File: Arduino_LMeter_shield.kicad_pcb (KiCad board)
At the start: 2 copper layers, 68.6 x 53.3 mm, 33 parts, among them J1 Lx, J2 Lx, J3 GPS, M1 OLED 1.3", Q1 2SC3356, SW1 Calib., U1 LTC8741, U2 74HC590

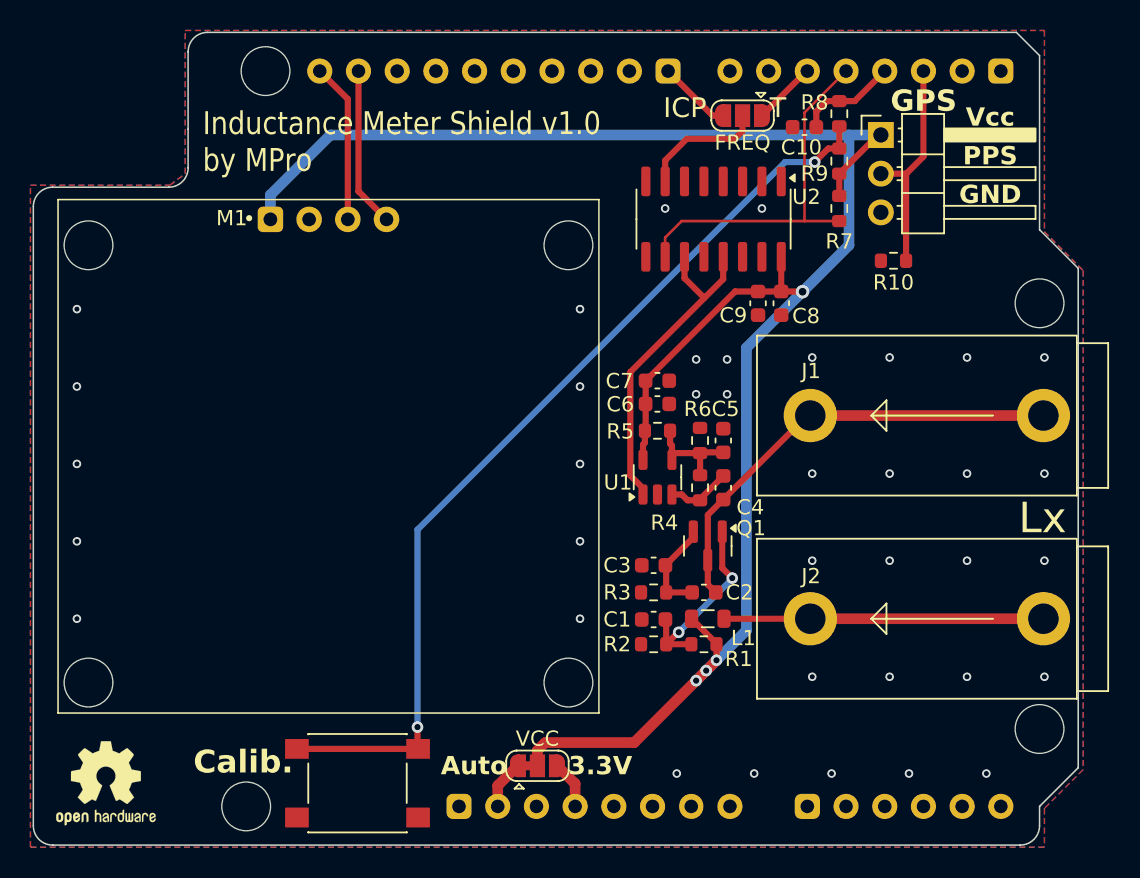
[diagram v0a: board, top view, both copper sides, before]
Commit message: OLED display footprint improved, 74HC590 chip LCSC index changed
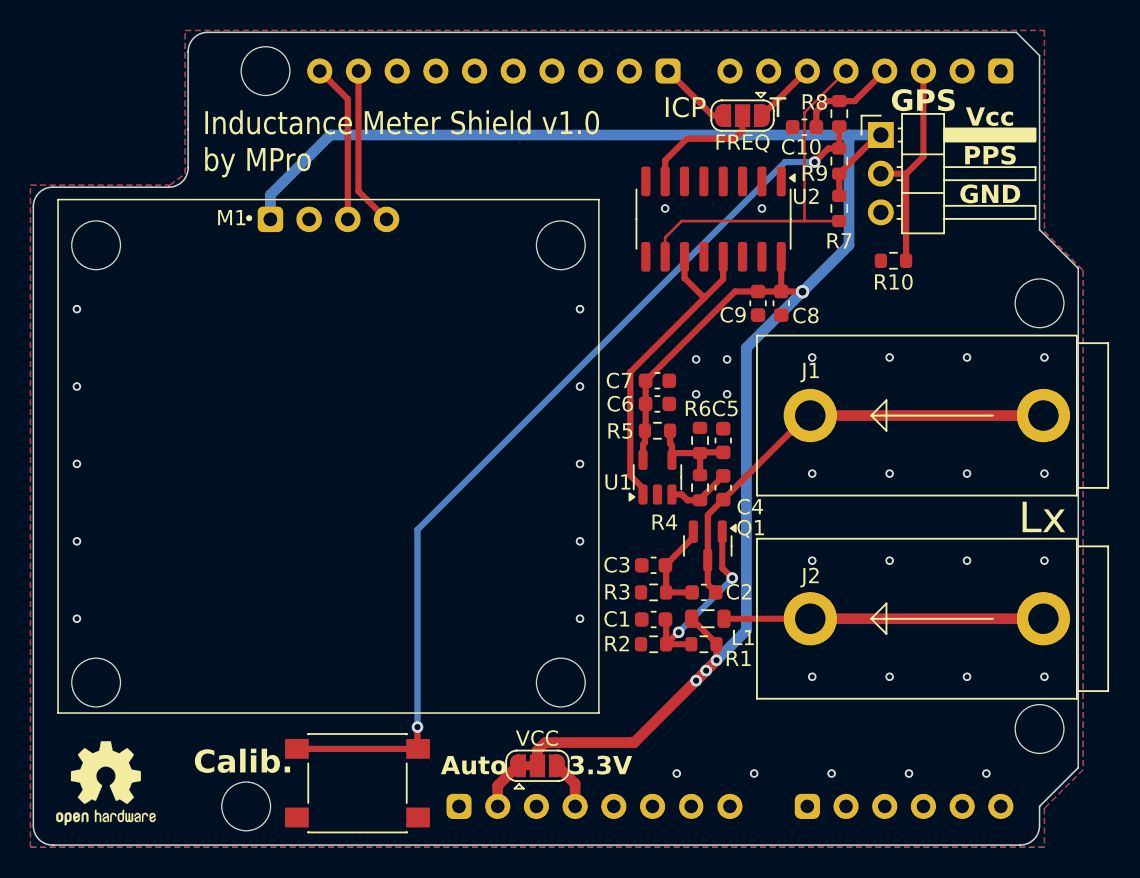
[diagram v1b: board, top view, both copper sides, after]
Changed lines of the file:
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@@
 	(title_block
 		(title "Arduino Inductance Meter shield")
-		(date "2025-04-17")
+		(date "2025-07-23")
 		(rev "1.0")
 		(company "© 2025 MPro")
@@
 		(sheetname "/")
 		(sheetfile "Arduino_LMeter_shield.kicad_sch")
-		(attr through_hole exclude_from_bom)
+		(attr through_hole exclude_from_pos_files exclude_from_bom)
 		(fp_line
 			(start 0 8.89)
@@
 			)
 		)
-		(property "Datasheet" ""
+		(property "Datasheet" "~"
 			(at 0 0 90)
 			(layer "F.Fab")
@@
 			)
 		)
-		(property "Datasheet" ""
+		(property "Datasheet" "~"
 			(at 0 0 0)
 			(layer "F.Fab")
@@
 			)
 		)
-		(property "Datasheet" ""
+		(property "Datasheet" "~"
 			(at 0 0 90)
 			(layer "F.Fab")
@@
 			)
 		)
-		(property "Datasheet" ""
+		(property "Datasheet" "~"
 			(at 0 0 0)
 			(layer "F.Fab")
@@
 			)
 		)
-		(property "Datasheet" ""
+		(property "Datasheet" "~"
 			(at 0 0 180)
 			(unlocked yes)
@@
 			)
 		)
-		(property "Datasheet" ""
+		(property "Datasheet" "~"
 			(at 0 0 0)
 			(layer "F.Fab")
@@
 			)
 		)
-		(property "Datasheet" ""
+		(property "Datasheet" "~"
 			(at 0 0 0)
 			(layer "F.Fab")
@@
 			)
 		)
-		(property "Datasheet" ""
+		(property "Datasheet" "~"
 			(at 0 0 0)
 			(layer "F.Fab")
@@
 			)
 		)
-		(property "Datasheet" ""
+		(property "Datasheet" "~"
 			(at 0 0 0)
 			(layer "F.Fab")
@@
 			)
 		)
-		(property "Datasheet" ""
+		(property "Datasheet" "~"
 			(at 0 0 90)
 			(layer "F.Fab")
@@
 			)
 		)
-		(property "Datasheet" ""
+		(property "Datasheet" "~"
 			(at 0 0 0)
 			(layer "F.Fab")
@@
 			)
 		)
-		(property "Datasheet" ""
+		(property "Datasheet" "~"
 			(at 0 0 0)
 			(layer "F.Fab")
@@
 			)
 		)
-		(property "Datasheet" ""
+		(property "Datasheet" "~"
 			(at 0 0 0)
 			(layer "F.Fab")
@@
 			)
 		)
-		(property "Datasheet" ""
+		(property "Datasheet" "~"
 			(at 0 0 0)
 			(unlocked yes)
@@
 			)
 		)
-		(property "Datasheet" ""
+		(property "Datasheet" "~"
 			(at 0 0 0)
 			(layer "F.Fab")
@@
 			)
 		)
-		(property "Datasheet" ""
+		(property "Datasheet" "~"
 			(at 0 0 0)
 			(layer "F.Fab")
@@
 			)
 		)
-		(property "Datasheet" ""
+		(property "Datasheet" "~"
 			(at 0 0 0)
 			(layer "F.Fab")
@@
 			)
 		)
-		(property "Datasheet" ""
+		(property "Datasheet" "~"
 			(at 0 0 90)
 			(layer "F.Fab")
@@
 			)
 		)
-		(property "LCSC" "C2652997"
+		(property "LCSC" "C547118"
 			(at 0 0 270)
 			(unlocked yes)
@@
 			)
 		)
-		(property "Datasheet" ""
+		(property "Datasheet" "~"
 			(at 0 0 0)
 			(layer "F.Fab")
@@
 		)
 		(pad "" np_thru_hole circle
-			(at -15.75 -14.35)
+			(at -15.25 -14.35)
 			(size 3 3)
 			(drill 3.2)
@@
 		)
 		(pad "" np_thru_hole circle
-			(at -15.75 14.35)
+			(at -15.25 14.35)
 			(size 3 3)
 			(drill 3.2)
@@
 		)
 		(pad "" np_thru_hole circle
-			(at 15.75 -14.35)
+			(at 15.25 -14.35)
 			(size 3 3)
 			(drill 3.2)
@@
 		)
 		(pad "" np_thru_hole circle
-			(at 15.75 14.35)
+			(at 15.25 14.35)
 			(size 3 3)
 			(drill 3.2)
@@
 		(model "${KIPRJMOD}/shapes3D/hex spacer standoff nut_M3 L8.stpZ"
 			(offset
-				(xyz -15.75 14.35 0)
+				(xyz 15.25 14.35 0)
 			)
 			(scale
-				(xyz 1 1 0.8)
+				(xyz 1 1 0.81)
 			)
 			(rotate
@@
 		(model "${KIPRJMOD}/shapes3D/hex spacer standoff nut_M3 L8.stpZ"
 			(offset
-				(xyz 15.75 14.35 0)
+				(xyz 15.25 -14.35 0)
 			)
 			(scale
-				(xyz 1 1 0.8)
+				(xyz 1 1 0.81)
 			)
 			(rotate
@@
 		(model "${KIPRJMOD}/shapes3D/hex spacer standoff nut_M3 L8.stpZ"
 			(offset
-				(xyz -15.75 -14.35 0)
+				(xyz -15.25 14.35 0)
 			)
 			(scale
-				(xyz 1 1 0.8)
+				(xyz 1 1 0.81)
 			)
 			(rotate
@@
 		(model "${KIPRJMOD}/shapes3D/hex spacer standoff nut_M3 L8.stpZ"
 			(offset
-				(xyz 15.75 -14.35 0)
+				(xyz -15.25 -14.35 0)
 			)
 			(scale
-				(xyz 1 1 0.8)
+				(xyz 1 1 0.81)
 			)
 			(rotate
@@
 			)
 		)
-		(property "Datasheet" ""
+		(property "Datasheet" "~"
 			(at 0 0 0)
 			(layer "F.Fab")
@@
 			)
 		)
-		(property "Datasheet" ""
+		(property "Datasheet" "~"
 			(at 0 0 90)
 			(layer "F.Fab")
@@
 			)
 		)
-		(property "Datasheet" ""
+		(property "Datasheet" "~"
 			(at 0 0 0)
 			(unlocked yes)
@@
 			)
 		)
-		(property "Datasheet" ""
+		(property "Datasheet" "~"
 			(at 0 0 0)
 			(layer "F.Fab")
@@
 			)
 		)
-		(property "Datasheet" ""
+		(property "Datasheet" "~"
 			(at 0 0 90)
 			(layer "F.Fab")
@@
 			)
 		)
-		(property "Datasheet" ""
+		(property "Datasheet" "~"
 			(at 0 0 0)
 			(layer "F.Fab")
@@
 			)
 		)
-		(property "Datasheet" ""
+		(property "Datasheet" "~"
 			(at 0 0 0)
 			(layer "F.Fab")
@@
 			)
 		)
-		(property "Datasheet" ""
+		(property "Datasheet" "~"
 			(at 0 0 90)
 			(layer "F.Fab")
@@
 			)
 		)
-		(property "Datasheet" ""
+		(property "Datasheet" "~"
 			(at 0 0 90)
 			(layer "F.Fab")
@@
 			)
 		)
-		(property "Datasheet" ""
+		(property "Datasheet" "~"
 			(at 0 0 90)
 			(layer "F.Fab")
